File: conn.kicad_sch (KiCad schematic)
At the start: 48 parts, among them J401 PWR IN, J402 Toolhead 1, J403 Toolhead 2, J405 IN, J406 OUT, J407 OUT, Q401 CJAC70P06, Q403 AO3400A, Q404 CJAC70P06, Q405 AO3400A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

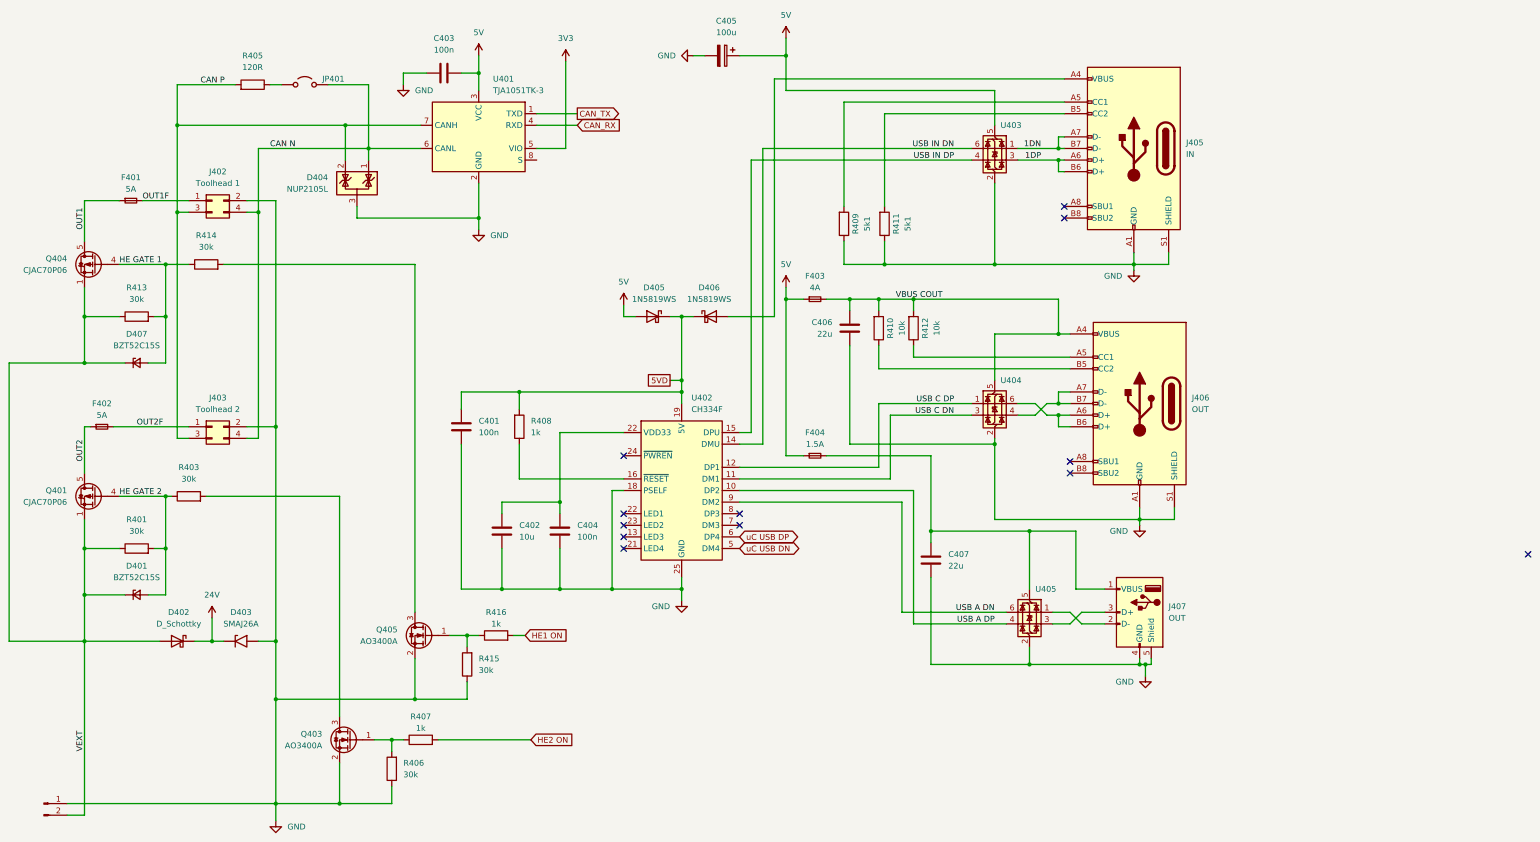
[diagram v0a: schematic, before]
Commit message: Rev 0.2: Major hardware improvements and production readiness
Hardware Improvements (Thanks to shx for schematic cleanup):
- Clean up schematic organization and structure
- Set CAN transceiver Silent pin to GND for stability
- Add status LEDs (yellow: 24V/5V/3.3V, green: MCU PB4)
- Replace jumpers with solder jumpers on bottom side
- Add jumpers to output PFETs for permanent-on without firmware
- Add robust test points for 5V/GND load testing
- Add optional heatsink for DC/DC converter on bottom
- Add 10µF capacitor for MCU on 3.3V rail

Component Optimizations:
- Replace 30kΩ with 33kΩ basic part for simplified BOM
- Change DC/DC feedback: 15.5kΩ15kΩ (new output: 5.1V)
- Upgrade CAN ESD protection: NUP2105LPESD1CAN
- Increase CAN termination resistor footprint: 04020603
- Switch USB hub supply from 5V to 3.3V per datasheet

Production Ready:
- Add all LCSC part numbers and rotations
- Generate complete production data package
- Improve PCB layout and button placement
- Create comprehensive changelog documentation
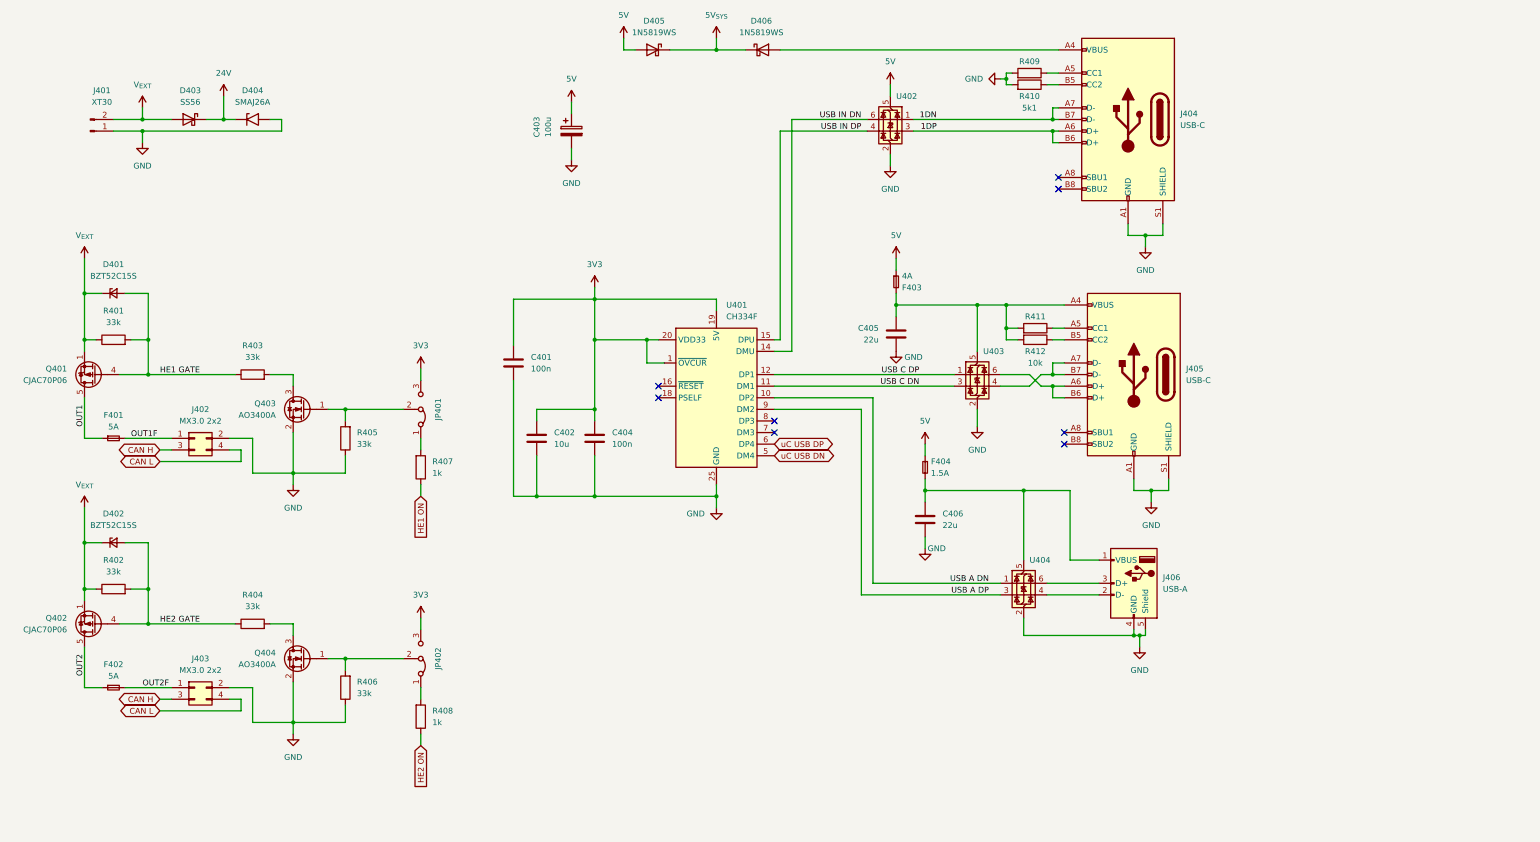
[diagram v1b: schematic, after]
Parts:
- removed C403: 100n, Capacitor_SMD:C_0402_1005Metric, symbol Device:C
- removed D404: NUP2105L, Package_TO_SOT_SMD:SOT-23, symbol Power_Protection:NUP2105L
- removed JP401: ~, Connector_PinHeader_2.54mm:PinHeader_1x02_P2.54mm_Vertical, symbol Jumper:Jumper_2_Open
- removed R405: 120R, Resistor_SMD:R_0402_1005Metric_Pad0.72x0.64mm_HandSolder, symbol Device:R
- removed R416: 1k, Resistor_SMD:R_0402_1005Metric, symbol Device:R
- removed U401: TJA1051TK-3, Package_SON:HVSON-8-1EP_3x3mm_P0.65mm_EP1.6x2.4mm, symbol Interface_CAN_LIN:TJA1051TK-3
- added JP401, JP402: ~, project:SolderJumper-3_P1.3mm_Bridged12_RoundedPad1.0x1.5mm_custom, symbol Jumper:Jumper_3_Bridged12
- C401, C404: LCSC Part # (none) -> C307331; Manufacturer Part # (none) -> CL05B104KB54PNC
- C402: LCSC Part # (none) -> C96446; Manufacturer Part # (none) -> CL10A106MA8NRNC
- C405: renamed from C406; LCSC Part # (none) -> C12891; Manufacturer Part # (none) -> CL31A226KAHNNNE
- C406: renamed from C407; LCSC Part # (none) -> C12891; Manufacturer Part # (none) -> CL31A226KAHNNNE
- D403: renamed from D402; value D_Schottky -> SS56; LCSC Part # (none) -> C24138; Manufacturer Part # (none) -> SS56C
- D404: renamed from D403; LCSC Part # (none) -> C19077543; Manufacturer Part # (none) -> SMAJ26A
- D405, D406: LCSC Part # (none) -> C191023; Manufacturer Part # (none) -> 1N5819WS
- F401, F402: LCSC Part # (none) -> C163128; Manufacturer Part # (none) -> CFS12V3T5R0
- F403: LCSC Part # C49305071 -> C2680546; Manufacturer Part # BSMD0805L-400 -> JK-SMD-0805-400L-12
- J401: value PWR IN -> XT30; FT Rotation Offset (none) -> 180; LCSC Part # (none) -> C431092; Manufacturer Part # (none) -> XT30PW-M30.G.Y
- J402: value Toolhead 1 -> MX3.0 2x2; FT Rotation Offset (none) -> 180; LCSC Part # (none) -> C122413; Manufacturer Part # (none) -> 430450400
- J403: value Toolhead 2 -> MX3.0 2x2; FT Rotation Offset (none) -> 180; LCSC Part # (none) -> C122413; Manufacturer Part # (none) -> 430450400
- J404: renamed from J405; value IN -> USB-C
- J405: renamed from J406; value OUT -> USB-C
- J406: renamed from J407; value OUT -> USB-A
- Q401: renamed from Q404; FT Rotation Offset (none) -> 270; LCSC Part # (none) -> C2898279; Manufacturer Part # (none) -> CJAC70P06
- Q402: renamed from Q401; FT Rotation Offset (none) -> 270; LCSC Part # (none) -> C2898279; Manufacturer Part # (none) -> CJAC70P06
- Q403: renamed from Q405; LCSC Part # (none) -> C20917; Manufacturer Part # (none) -> AO3400A
- Q404: renamed from Q403; LCSC Part # (none) -> C20917; Manufacturer Part # (none) -> AO3400A
- R401: renamed from R413; value 30k -> 33k; LCSC Part # (none) -> C25779; Manufacturer Part # (none) -> 0402WGF3302TCE
- R402: renamed from R401; value 30k -> 33k; LCSC Part # (none) -> C25779; Manufacturer Part # (none) -> 0402WGF3302TCE
- R403: renamed from R414; value 30k -> 33k; LCSC Part # (none) -> C25779; Manufacturer Part # (none) -> 0402WGF3302TCE
- R404: renamed from R403; value 30k -> 33k; LCSC Part # (none) -> C25779; Manufacturer Part # (none) -> 0402WGF3302TCE
- R405: renamed from R415; value 30k -> 33k; LCSC Part # (none) -> C25779; Manufacturer Part # (none) -> 0402WGF3302TCE
- R406: value 30k -> 33k; LCSC Part # (none) -> C25779; Manufacturer Part # (none) -> 0402WGF3302TCE
- R407, R408: LCSC Part # (none) -> C11702; Manufacturer Part # (none) -> 0402WGF1001TCE
- R409: LCSC Part # (none) -> C25905; Manufacturer Part # (none) -> 0402WGF5101TCE
- R410: renamed from R411; LCSC Part # (none) -> C25905; Manufacturer Part # (none) -> 0402WGF5101TCE
- R411: renamed from R412; LCSC Part # (none) -> C25744; Manufacturer Part # (none) -> 0402WGF1002TCE
- R412: renamed from R410; LCSC Part # (none) -> C25744; Manufacturer Part # (none) -> 0402WGF1002TCE
- U401: renamed from U402; LCSC Part # (none) -> C5187527; Manufacturer Part # (none) -> CH334F
- U402: renamed from U403; FT Rotation Offset (none) -> 90; LCSC Part # (none) -> C2687116; Manufacturer Part # (none) -> USBLC6-2SC6
- U403: renamed from U404; FT Rotation Offset (none) -> 90; LCSC Part # (none) -> C2687116; Manufacturer Part # (none) -> USBLC6-2SC6
- U404: renamed from U405; FT Rotation Offset (none) -> 90; LCSC Part # (none) -> C2687116; Manufacturer Part # (none) -> USBLC6-2SC6
- renumbered C405 to C403, D407 to D401, D401 to D402
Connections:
- net 3V3: now also C401.1, C402.1, C404.1, U401.1 (~{OVCUR}), U401.19 (5V), U401.20 (VDD33), JP401.3 (B), JP402.3 (B)
- net GND: now also R409.2, R410.2; no longer R409.1, R410.1, U401.18 (PSELF)
- net HE1 ON: now also R407.1
- net HE2 ON: now also R408.1; no longer R407.2
- net USB A DN: now also U401.10 (DP2), U404.1 (I/O1); no longer U401.9 (DM2), U404.6 (I/O1)
- net USB A DP: now also U401.9 (DM2), U404.3 (I/O2); no longer U401.10 (DP2), U404.4 (I/O2)
- net at Q403.1 (G), R405.2: now also JP401.2 (C)
- net at Q404.1 (G), R406.2: now also JP402.2 (C); no longer R407.1
- net at J404.B5 (CC2): now also R410.1; no longer R410.2
- net at U401.16 (~{RESET}): no longer R408.1
- net at J406.2 (D-): now also U404.4 (I/O2); no longer U404.1 (I/O1)
- net at J406.3 (D+): now also U404.6 (I/O1); no longer U404.3 (I/O2)
- net at J404.A5 (CC1): now also R409.1; no longer R409.2
- removed net 5VD: C401.1, D405.1 (K), D406.1 (K), R408.2, U401.19 (5V)
- net CAN N renamed CAN L
- net CAN P renamed CAN H
- net HE GATE 1 renamed HE1 GATE
- net HE GATE 2 renamed HE2 GATE
- net VBUS COUT: no longer names the net of C405.1, F403.2, J405.A4 (VBUS), J405.A9 (VBUS), J405.B4 (VBUS), J405.B9 (VBUS), R411.2, R412.2, U403.5 (VBUS)
- net VEXT renamed V_{EXT}
- new net: JP401.1 (A), R407.2
- new net: JP402.1 (A), R408.2
- new net 5V_{SYS}: D405.1 (K), D406.1 (K)
- now unconnected: U401.22 (LED1)
- no-connect marks 12 -> 8
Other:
- moved on the sheet: C401, C402, C403, C404, C405, C406, D401, D402, D403, D404, D405, D406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
